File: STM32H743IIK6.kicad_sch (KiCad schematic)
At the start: 24 parts, among them J1 BAT_SW, SW1 SW_Push, U2 STM32H743IITx

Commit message: Added UART, i2c, debug, NAND Flash, NOR Flash, EEPROM, SD-Card
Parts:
- removed BT1: Battery_Cell, Battery:BatteryHolder_Keystone_1060_1x2032, symbol Device:Battery_Cell
- removed C1, C2: 2u2, Capacitor_SMD:C_0603_1608Metric, symbol Device:C
- removed C3: 100n, Capacitor_SMD:C_0201_0603Metric, symbol Device:C_Small
- removed J1: BAT_SW, Connector_PinHeader_2.54mm:PinHeader_1x03_P2.54mm_Vertical, symbol Connector_Generic:Conn_01x03
- removed R1, R2: 10K, Resistor_SMD:R_0402_1005Metric, symbol Device:R_Small
- removed SW1: SW_Push, Button_Switch_SMD:SW_SPST_PTS645, symbol Switch:SW_Push
- removed U2: STM32H743IITx, Package_QFP:LQFP-176_24x24mm_P0.5mm, symbol MCU_ST_STM32H7:STM32H743IITx
- added C34, C35: 2u2, Capacitor_SMD:C_0603_1608Metric, symbol Device:C
- added C39, C40: 10p, Capacitor_SMD:C_0402_1005Metric, symbol Device:C_Small
- added C41, C42: 22p, Capacitor_SMD:C_0402_1005Metric, symbol Device:C_Small
- added C43: 4n7, Capacitor_SMD:C_0402_1005Metric, symbol Device:C_Small
- added D2: PRTR5V0U2X, Package_TO_SOT_SMD:SOT-143, symbol Power_Protection:PRTR5V0U2X
- added J4: USB-C, Connector_USB:USB_C_Receptacle_G-Switch_GT-USB-7010ASV, symbol Connector:USB_C_Receptacle_USB2.0_16P
- added R11, R12: 5K1, Resistor_SMD:R_0402_1005Metric, symbol Device:R_Small
- added R13: 1M, Resistor_SMD:R_0402_1005Metric, symbol Device:R_Small
- added U4: STM32H723ZGTx, Package_QFP:LQFP-144_20x20mm_P0.5mm, symbol MCU_ST_STM32H7:STM32H723ZGTx
- added Y1: 25MHz, Crystal:Crystal_SMD_2520-4Pin_2.5x2.0mm, symbol Device:Crystal_GND24_Small
- added Y2: 32.768KHz, Crystal:Crystal_SMD_2012-2Pin_2.0x1.2mm, symbol Device:Crystal_Small
- C10, C11, C12, C13, C14, C15, C16, C17, C4, C5, C6, C7, C8, C9: footprint Capacitor_SMD:C_0201_0603Metric -> Capacitor_SMD:C_0402_1005Metric
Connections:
- net VDD is gone; now on net +3V3: C10.1, C11.1, C12.1, C13.1, C14.1, C15.1, C16.1, C17.1, C19.1, C4.1, C5.1, C6.1, C7.1, C8.1, C9.1
- net +3V3: now also U4.108 (VDD), U4.121 (VDD), U4.131 (VDD), U4.144 (VDD), U4.17 (VDD), U4.30 (VDD), U4.33 (VDDA), U4.39 (VDD), U4.52 (VDD), U4.6 (VBAT), U4.62 (VDD), U4.72 (VDD), U4.84 (VDD), U4.95 (VDD33USB)
- net GND: now also C34.2, C35.2, C39.2, C40.2, C41.2, C42.2, C43.2, D2.1 (GND), J4.A1 (GND), J4.A12 (GND), J4.B1 (GND), J4.B12 (GND), R11.1, R12.1, R13.2, U4.107 (VSS), U4.120 (VSS), U4.130 (VSS), U4.16 (VSS), U4.31 (VSSA), U4.38 (VSS), U4.51 (VSS), U4.61 (VSS), U4.83 (VSS), U4.94 (VSS), Y1.2, Y1.4
- net PA0: now also U4.34 (PA0)
- net PA1: now also U4.35 (PA1)
- net PA10: now also U4.102 (PA10)
- net PA2: now also U4.36 (PA2)
- net PA3: now also U4.37 (PA3)
- net PA4: now also U4.40 (PA4)
- net PA5: now also U4.41 (PA5)
- net PA6: now also U4.42 (PA6)
- net PA7: now also U4.43 (PA7)
- net PA8: now also U4.100 (PA8)
- net PA9: now also U4.101 (PA9)
- net PB0: now also U4.46 (PB0)
- net PB1: now also U4.47 (PB1)
- net PB10: now also U4.69 (PB10)
- net PB11: now also U4.70 (PB11)
- net PB12: now also U4.73 (PB12)
- net PB13: now also U4.74 (PB13)
- net PB14: now also U4.75 (PB14)
- net PB15: now also U4.76 (PB15)
- net PB2: now also U4.48 (PB2)
- net PB5: now also U4.135 (PB5)
- net PB6: now also U4.136 (PB6)
- net PB7: now also U4.137 (PB7)
- net PB8: now also U4.139 (PB8)
- net PB9: now also U4.140 (PB9)
- net PC1: now also U4.27 (PC1)
- net PC10: now also U4.111 (PC10)
- net PC11: now also U4.112 (PC11)
- net PC12: now also U4.113 (PC12)
- net PC13: now also U4.7 (PC13)
- net PC6: now also U4.96 (PC6)
- net PC7: now also U4.97 (PC7)
- net PC8: now also U4.98 (PC8)
- net PC9: now also U4.99 (PC9)
- net PD11: now also U4.80 (PD11)
- net PD12: now also U4.81 (PD12)
- net PD13: now also U4.82 (PD13)
- net PD2: now also U4.116 (PD2)
- net PD3: now also U4.117 (PD3)
- net PD4: now also U4.118 (PD4)
- net PD5: now also U4.119 (PD5)
- net PD6: now also U4.122 (PD6)
- net PD7: now also U4.123 (PD7)
- net PE2: now also U4.1 (PE2)
- net PE3: now also U4.2 (PE3)
- net PE4: now also U4.3 (PE4)
- net PE5: now also U4.4 (PE5)
- net PE6: now also U4.5 (PE6)
- net PF10: now also U4.22 (PF10)
- net PF6: now also U4.18 (PF6)
- net PF7: now also U4.19 (PF7)
- net PF8: now also U4.20 (PF8)
- net PF9: now also U4.21 (PF9)
- net PG10: now also U4.125 (PG10)
- net PG11: now also U4.126 (PG11)
- net PG12: now also U4.127 (PG12)
- net PG13: now also U4.128 (PG13)
- net PG14: now also U4.129 (PG14)
- net PG2: now also U4.87 (PG2)
- net PG3: now also U4.88 (PG3)
- net PG6: now also U4.91 (PG6)
- net PG7: now also U4.92 (PG7)
- net PG9: now also U4.124 (PG9)
- new net: C34.1, C35.1, U4.106 (VCAP), U4.71 (VCAP)
- new net: C43.1, J4.S1 (SHIELD), R13.1
- new net: J4.A5 (CC1), R11.2
- new net: J4.B5 (CC2), R12.2
- new net A0: U4.10 (PF0)
- new net A1: U4.11 (PF1)
- new net A10: U4.56 (PG0)
- new net A11: U4.57 (PG1)
- new net A2: U4.12 (PF2)
- new net A3: U4.13 (PF3)
- new net A4: U4.14 (PF4)
- new net A5: U4.15 (PF5)
- new net A6: U4.50 (PF12)
- new net A7: U4.53 (PF13)
- new net A8: U4.54 (PF14)
- new net A9: U4.55 (PF15)
- new net BA0: U4.89 (PG4)
- new net BA1: U4.90 (PG5)
- new net BOOT0: U4.138 (BOOT0)
- new net DQ0: U4.85 (PD14)
- new net DQ1: U4.86 (PD15)
- new net DQ10: U4.66 (PE13)
- new net DQ11: U4.67 (PE14)
- new net DQ12: U4.68 (PE15)
- new net DQ13: U4.77 (PD8)
- new net DQ14: U4.78 (PD9)
- new net DQ15: U4.79 (PD10)
- new net DQ2: U4.114 (PD0)
- new net DQ3: U4.115 (PD1)
- new net DQ4: U4.58 (PE7)
- new net DQ5: U4.59 (PE8)
- new net DQ6: U4.60 (PE9)
- new net DQ7: U4.63 (PE10)
- new net DQ8: U4.64 (PE11)
- new net DQ9: U4.65 (PE12)
- new net OSC32_IN: C42.1, U4.8 (PC14), Y2.2
- new net OSC32_OUT: C41.1, U4.9 (PC15), Y2.1
- new net PA13(JTMS: U4.105 (PA13(JTMS)
- new net PA14(JTCK: U4.109 (PA14(JTCK)
- new net PA15(JTDI): U4.110 (PA15(JTDI))
- new net PB3(JTDO: U4.133 (PB3(JTDO)
- new net PB4(NJTRST): U4.134 (PB4(NJTRST))
- new net PC2_C: U4.28 (PC2_C)
- new net PC3_C: U4.29 (PC3_C)
- new net SDRAM_CKE: U4.45 (PC5)
- new net SDRAM_CLK: U4.93 (PG8)
- new net SDRAM_LDQM: U4.141 (PE0)
- new net SDRAM_UDQM: U4.142 (PE1)
- new net USB_D+: D2.3 (I/O2), J4.A6 (D+), J4.B6 (D+), U4.104 (PA12)
- new net USB_D-: D2.2 (I/O1), J4.A7 (D-), J4.B7 (D-), U4.103 (PA11)
- new net VBUS: J4.A4 (VBUS), J4.A9 (VBUS), J4.B4 (VBUS), J4.B9 (VBUS)
- new net XIN: C39.1, U4.23 (PH0), Y1.3
- new net XOUT: C40.1, U4.24 (PH1), Y1.1
- new net ~{SDRAM_CAS}: U4.132 (PG15)
- new net ~{SDRAM_CS}: U4.44 (PC4)
- new net ~{SDRAM_RAS}: U4.49 (PF11)
- new net ~{SDRAM_WE}: U4.26 (PC0)
- no-connect marks 0 -> 2
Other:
- moved on the sheet: C10, C11, C12, C13, C14, C15, C16, C17, C19, C4, C5, C6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

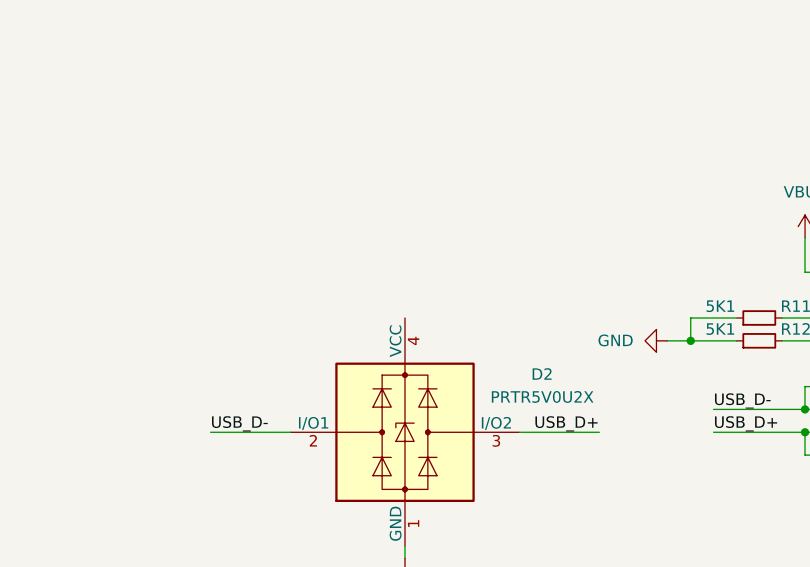
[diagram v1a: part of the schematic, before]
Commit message: Added I2S Audio amplifier
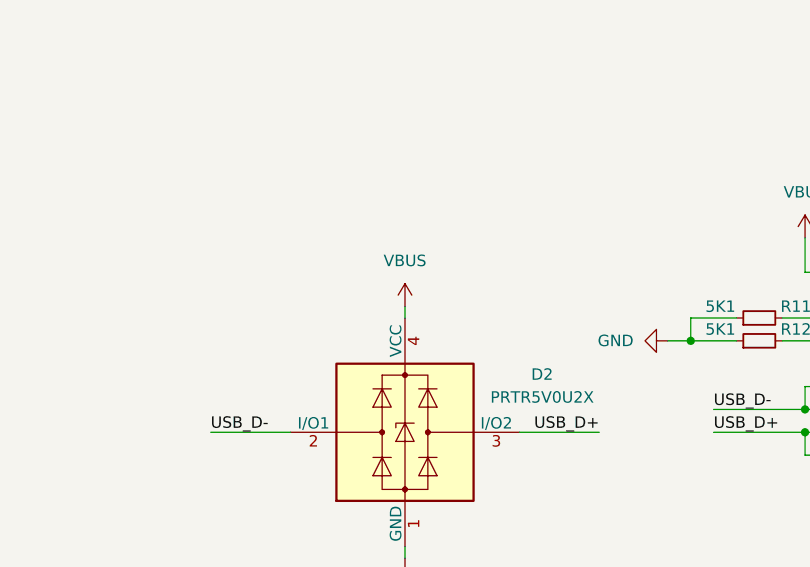
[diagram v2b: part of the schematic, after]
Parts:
- C10, C11, C12, C13, C14, C15, C16, C17, C4, C5, C6, C7, C8, C9: footprint Capacitor_SMD:C_0402_1005Metric -> Capacitor_SMD:C_0201_0603Metric
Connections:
- net VBUS: now also D2.4 (VCC)

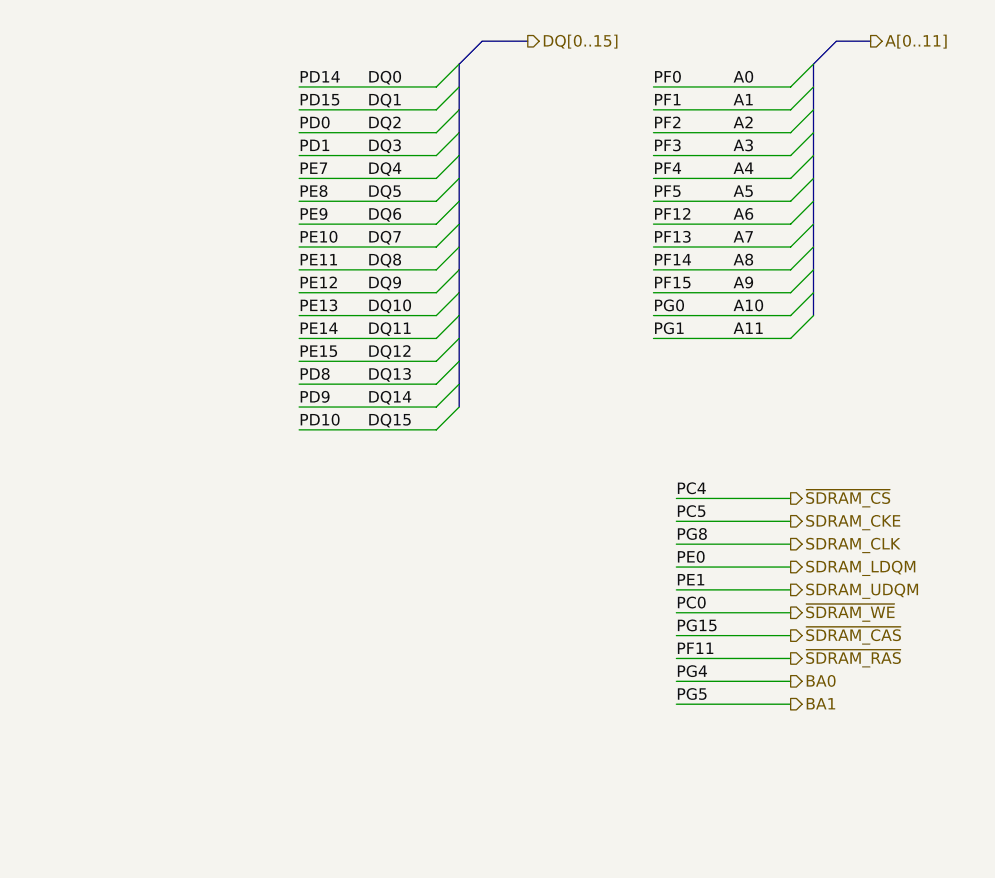
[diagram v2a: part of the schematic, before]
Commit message: Finish high speed sdram tracks
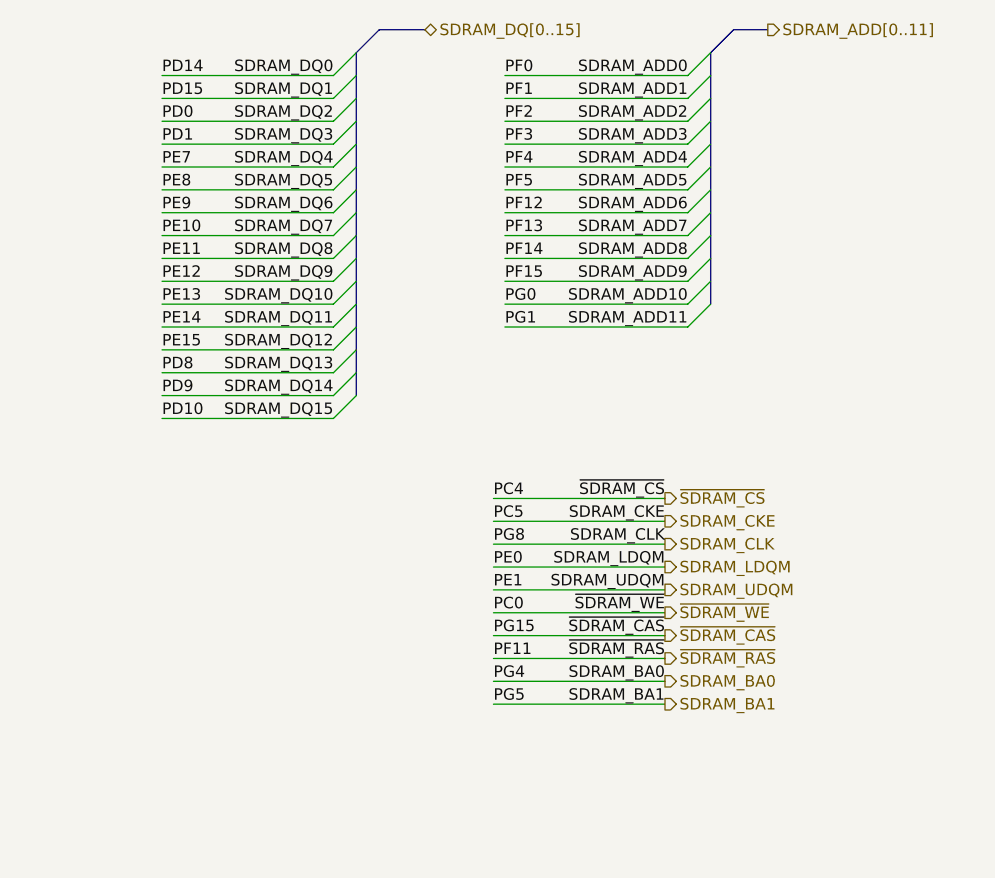
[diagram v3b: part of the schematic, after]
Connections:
- net A0 renamed PF0
- net A1 renamed PF1
- net A10 renamed PG0
- net A11 renamed PG1
- net A2 renamed PF2
- net A3 renamed PF3
- net A4 renamed PF4
- net A5 renamed PF5
- net A6 renamed PF12
- net A7 renamed PF13
- net A8 renamed PF14
- net A9 renamed PF15
- net BA0 renamed SDRAM_BA0
- net BA1 renamed SDRAM_BA1
- net DQ0 renamed PD14
- net DQ1 renamed PD15
- net DQ10 renamed PE13
- net DQ11 renamed PE14
- net DQ12 renamed PE15
- net DQ13 renamed PD8
- net DQ14 renamed PD9
- net DQ15 renamed PD10
- net DQ2 renamed PD0
- net DQ3 renamed PD1
- net DQ4 renamed PE7
- net DQ5 renamed PE8
- net DQ6 renamed PE9
- net DQ7 renamed PE10
- net DQ8 renamed PE11
- net DQ9 renamed PE12

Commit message: Finish sdram, LCD, SD-card, QSPI, I2S tracks
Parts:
- added C24, C25, C27, C28: 100n, Capacitor_SMD:C_0402_1005Metric, symbol Device:C_Small
- added C26: 1u, Capacitor_SMD:C_0603_1608Metric, symbol Device:C
- added C30: 1u, Capacitor_SMD:C_0805_2012Metric, symbol Device:C
- added C44: 2.2u, Capacitor_SMD:C_0805_2012Metric, symbol Device:C
- added C45: 10u, Capacitor_SMD:C_0805_2012Metric, symbol Device:C
- added D3: NSR0340HT1G, Diode_SMD:D_SOD-323, symbol Diode:NSR0340HT1G
- added D4, D5, D6: LED, LED_SMD:LED_0805_2012Metric, symbol Device:LED
- added R17, R18, R19, R20: 10K, Resistor_SMD:R_0402_1005Metric, symbol Device:R_Small
- added R21: 2K2, Resistor_SMD:R_0402_1005Metric, symbol Device:R_Small
- added R22: 100K, Resistor_SMD:R_0402_1005Metric, symbol Device:R_Small
- added R23, R24: 1K, Resistor_SMD:R_0402_1005Metric, symbol Device:R_Small
- added SW1, SW2, SW3, SW4: SW_Push, Button_Switch_SMD:SW_SPST_PTS810, symbol Switch:SW_Push
- added U8: TLV75733PDBV, Package_TO_SOT_SMD:SOT-23-5, symbol Regulator_Linear:TLV75733PDBV
- C10, C11, C12, C13, C14, C15, C16, C17, C4, C5, C6, C7, C8, C9: footprint Capacitor_SMD:C_0201_0603Metric -> Capacitor_SMD:C_0402_1005Metric
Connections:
- net +3V3: now also U4.32 (VREF+), C25.1, C26.1, C44.1, R17.1, R19.1, R21.1, SW2.2, U8.5 (OUT)
- net BOOT0: now also R18.1, SW2.1
- net GND: now also C24.2, C25.2, C26.2, C27.2, C28.2, C30.2, C44.2, C45.2, D4.1 (K), D5.1 (K), D6.1 (K), R18.2, R22.2, SW1.2, SW3.2, SW4.2, U8.2 (GND)
- net VBUS: now also C45.1, D3.2 (A), R22.1
- net at U4.143 (PDR_ON): now also R19.2
- net NRST: now reaches U4.25 (NRST)
- net NRST: now also C24.1, R17.2, SW1.1
- net PA0 renamed SD_CMD
- net PA10 renamed LTDC_B4
- net PA15(JTDI) renamed LTDC_B6
- net PA4 renamed I2S_WS
- net PA5 renamed LTDC_R4
- net PA6 renamed LTDC_G2
- net PA7 renamed LTDC_VSYNC
- net PA8 renamed LTDC_B3
- net PA9 renamed LTDC_R5
- net PB0 renamed LTDC_R3
- net PB1 renamed LTDC_R6
- net PB10 renamed LTDC_G4
- net PB11 renamed LTDC_G5
- net PB2 renamed NOR_CLK
- net PB3(JTDO renamed SD_DAT2
- net PB4(NJTRST) renamed LCD_TP_INT
- net PB5 renamed LTDC_B5
- net PB6 renamed LCD_TP_SCL
- net PB7 renamed LCD_TP_SDA
- net PB9 renamed LTDC_B7
- net PC1 renamed SD_CLK
- net PC11 renamed ~{NOR_CS}
- net PC13 renamed LCS_SPI_CS
- net PC6 renamed LTDC_HSYNC
- net PC7 renamed LTDC_G6
- net PC9 renamed LTDC_G3
- net PD11 renamed I2S_SD_MODE
- net PD3 renamed LTDC_G7
- net PD4 renamed NOR_D0
- net PD5 renamed NOR_D1
- net PD6 renamed NOR_D2
- net PD7 renamed I2S_SDO
- net PE4 renamed LCD_TP_RST
- net PF10 renamed LTDC_DE
- net PF6 renamed LCD_RESET
- net PF7 renamed LCS_SPI_CLK
- net PF9 renamed LCS_SPI_DAT
- net PG10 renamed SD_DAT1
- net PG11 renamed I2S_CK
- net PG12 renamed SD_DAT3
- net PG13 renamed SD_DET
- net PG14 renamed NOR_D3
- net PG6 renamed LTDC_R7
- net PG7 renamed LTDC_CLK
- net PG9 renamed SD_DAT0
- new net: R20.2, U8.3 (EN)
- new net: D6.2 (A), R24.2
- new net: D5.2 (A), R23.2
- new net: D4.2 (A), R21.2
- new net BTN0: C27.1, SW3.1
- new net BTN1: C28.1, SW4.1
- new net LED_0: R23.1
- new net LED_1: R24.1
- new net VDD: C30.1, D3.1 (K), R20.1, U8.1 (IN)
